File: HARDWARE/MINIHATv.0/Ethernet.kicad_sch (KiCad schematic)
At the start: 15 parts, among them J1 RJ45_Hanrun_HR911105A_Horizon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, U1 LAN8742A, Y1 Crystal_GND24_Small

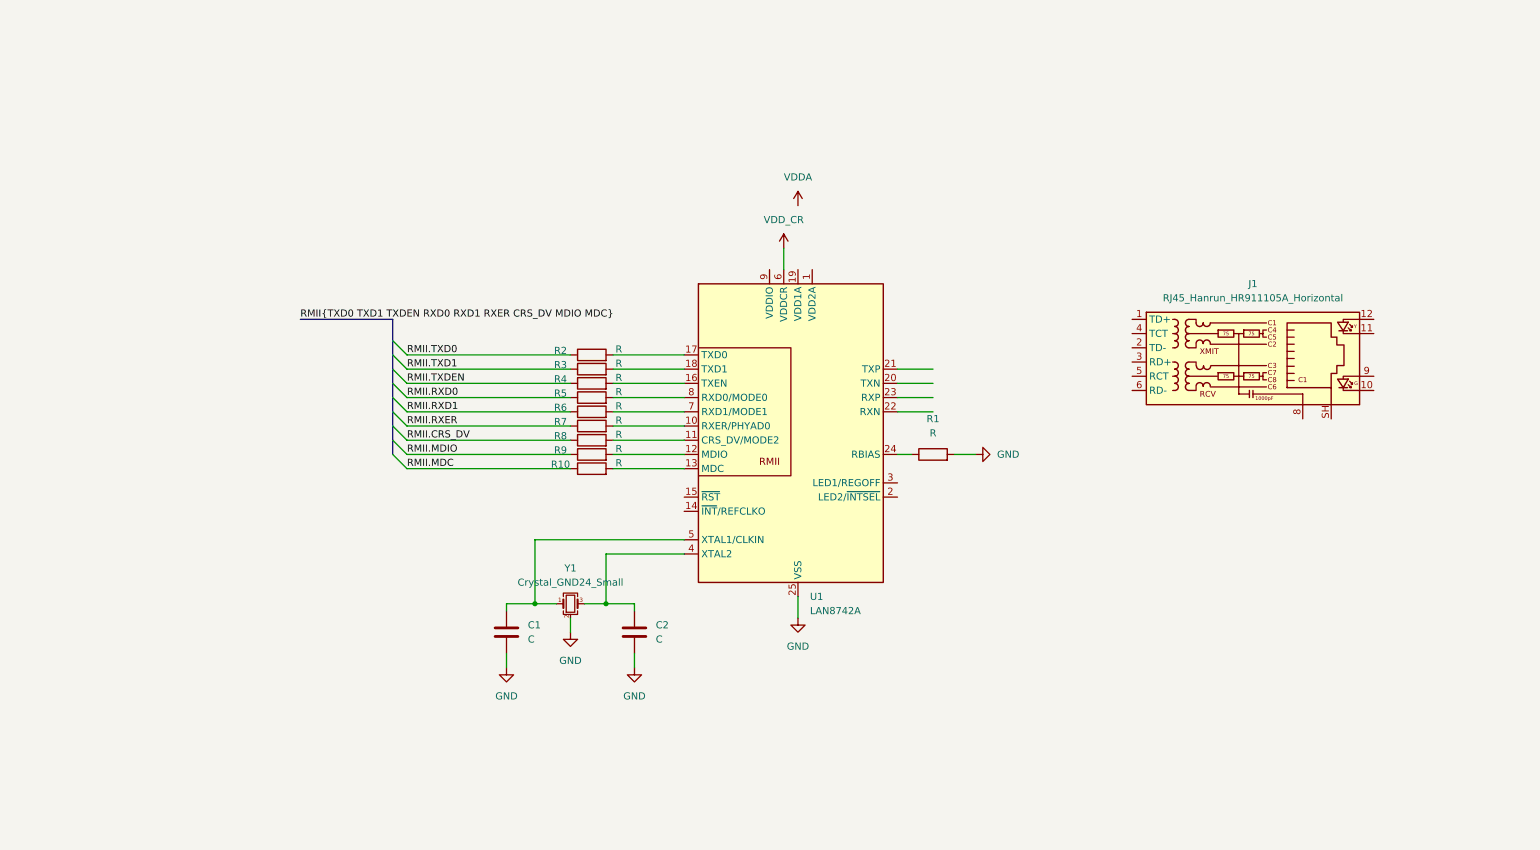
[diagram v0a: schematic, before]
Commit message: ethernet schematic complete
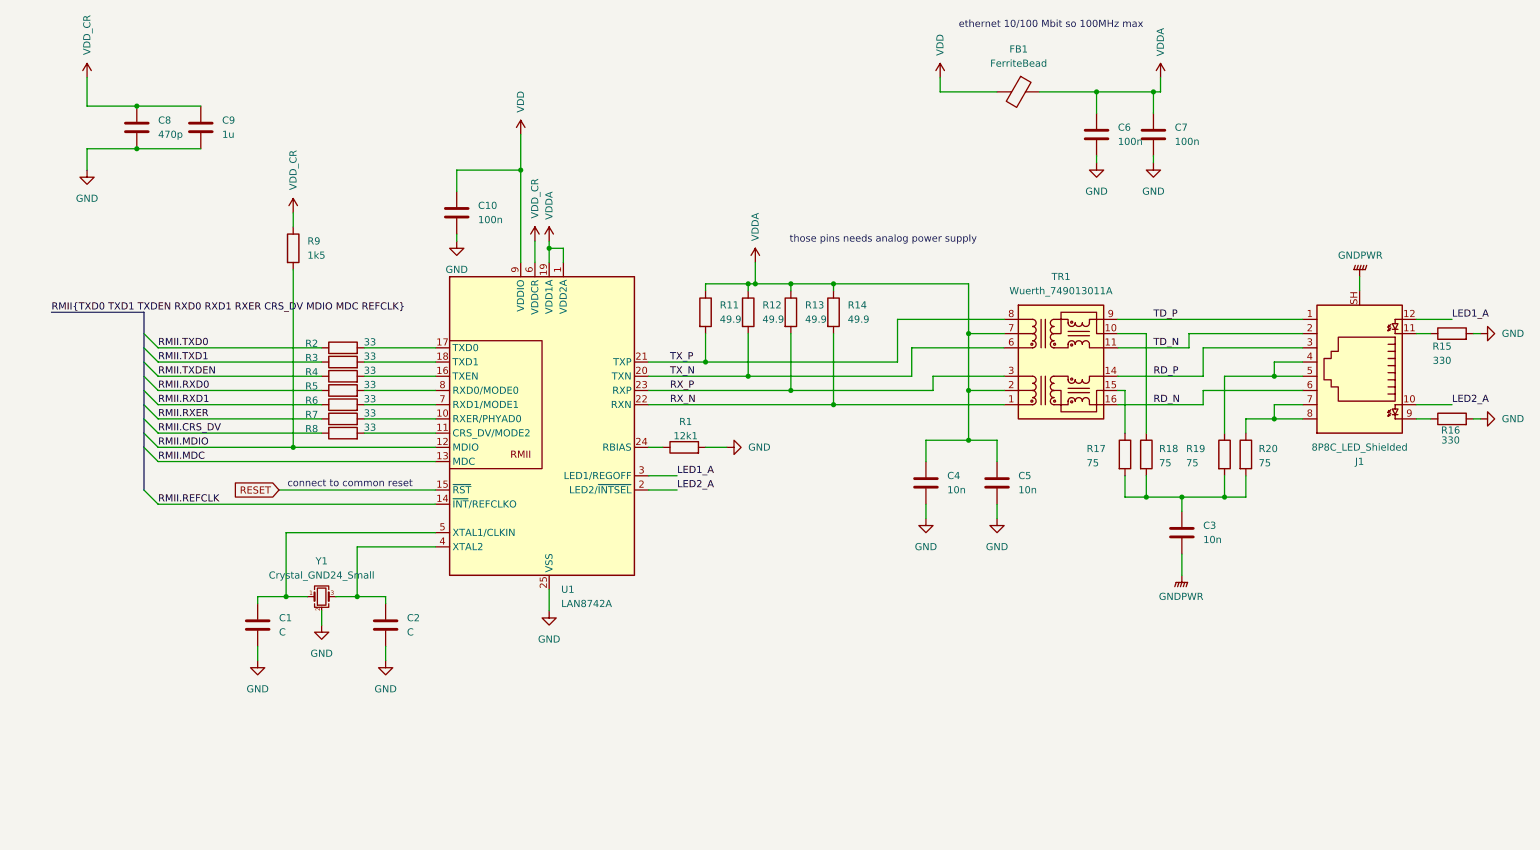
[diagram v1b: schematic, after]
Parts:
- removed J1: RJ45_Hanrun_HR911105A_Horizontal, Connector_RJ:RJ45_Amphenol_RJHSE538X, symbol Connector:RJ45_Hanrun_HR911105A_Horizontal
- removed R10: R, symbol Device:R
- added C10, C6, C7: 100n, symbol Device:C
- added C3, C4, C5: 10n, symbol Device:C
- added C8: 470p, symbol Device:C
- added C9: 1u, symbol Device:C
- added FB1: FerriteBead, symbol Device:FerriteBead
- added J1: 8P8C_LED_Shielded, symbol Connector:8P8C_LED_Shielded
- added R11, R12, R13, R14: 49.9, symbol Device:R
- added R15, R16: 330, symbol Device:R
- added R17, R18, R19, R20: 75, symbol Device:R
- added TR1: Wuerth_749013011A, Transformer_SMD:Transformer_Ethernet_Wuerth_749013011A, symbol Transformer:Wuerth_749013011A
- R1: value R -> 12k1
- R2, R3, R4, R5, R6, R7, R8: value R -> 33
- R9: value R -> 1k5
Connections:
- net GND: now also C10.2, C4.2, C5.2, C6.2, C7.2, C8.2, C9.2, R15.2, R16.2
- net RMII.MDC: now also U1.13 (MDC)
- net RMII.MDIO: now also R9.2, U1.12 (MDIO); no longer R9.1
- net VDDA: now also U1.1 (VDD2A), U1.19 (VDD1A), C4.1, C5.1, C6.1, C7.1, FB1.1, R11.1, R12.1, R13.1, R14.1, TR1.2 (C_TD), TR1.7 (C_RD)
- net VDD_CR: now also R9.1, C8.1, C9.1
- net RMII.REFCLK: now reaches U1.14 (~{INT}/REFCLKO)
- net RESET: now reaches U1.15 (~{RST})
- net LED2_A: now reaches U1.2 (LED2/~{INTSEL})
- net LED2_A: now also J1.10
- net TX_N: now reaches U1.20 (TXN)
- net TX_N: now also R12.2, TR1.6 (RD+)
- net TX_P: now reaches U1.21 (TXP)
- net TX_P: now also R11.2, TR1.8 (RD-)
- net RX_N: now reaches U1.22 (RXN)
- net RX_N: now also R14.2, TR1.1 (TD+)
- net RX_P: now reaches U1.23 (RXP)
- net RX_P: now also R13.2, TR1.3 (TD-)
- net LED1_A: now reaches U1.3 (LED1/REGOFF)
- net LED1_A: now also J1.12
- net VDD: now reaches U1.9 (VDDIO)
- net VDD: now also C10.1, FB1.2
- new net: R18.1, TR1.10 (C_RX)
- new net: R17.1, TR1.15 (C_TX)
- new net: C3.1, R17.2, R18.2, R19.2, R20.2
- new net: J1.7, J1.8, R20.1
- new net: J1.4, J1.5, R19.1
- new net: J1.11, R15.1
- new net: J1.9, R16.1
- new net GNDPWR: C3.2, J1.SH
- new net RD_N: J1.6, TR1.16 (TX+)
- new net RD_P: J1.3, TR1.14 (TX-)
- new net TD_N: J1.2, TR1.11 (RX+)
- new net TD_P: J1.1, TR1.9 (RX-)
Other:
- note added: "connect to common reset"
- note added: "ethernet 10/100 Mbit so 100MHz max"
- note added: "those pins needs analog power supply"
- moved on the sheet: C1, C2, R1, R2, R3, R4, R5, R6, R7, R8, U1, Y1

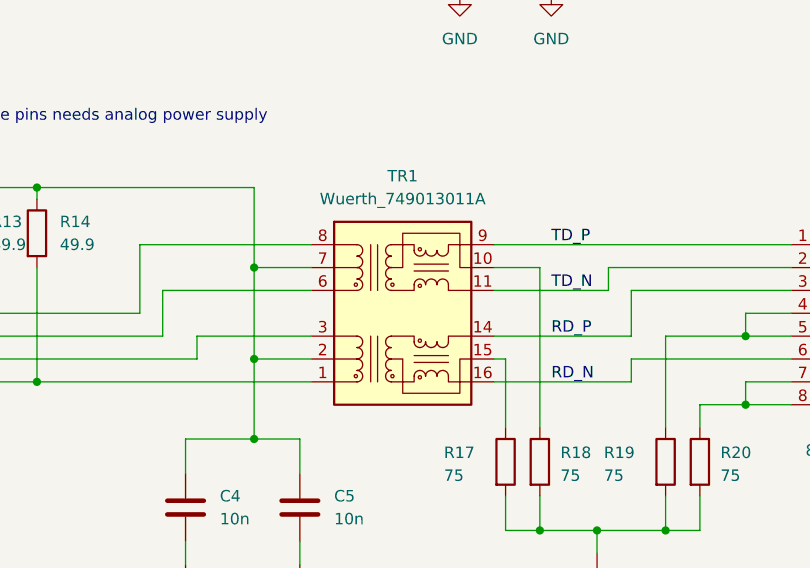
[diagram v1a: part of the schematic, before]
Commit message: added usb
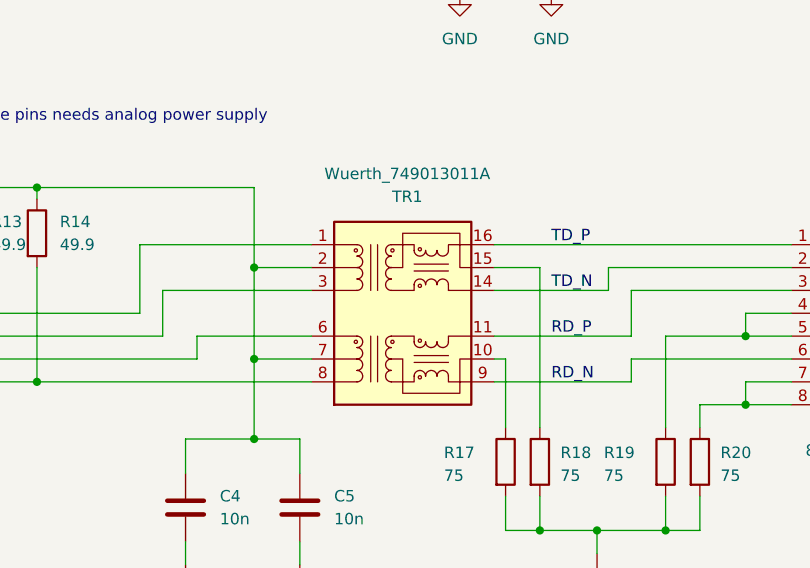
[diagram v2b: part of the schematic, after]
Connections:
- net RD_N: now also TR1.9 (RX-); no longer TR1.16 (TX+)
- net RD_P: now also TR1.11 (RX+); no longer TR1.14 (TX-)
- net RX_N: now also TR1.8 (RD-); no longer TR1.1 (TD+)
- net RX_P: now also TR1.6 (RD+); no longer TR1.3 (TD-)
- net TD_N: now also TR1.14 (TX-); no longer TR1.11 (RX+)
- net TD_P: now also TR1.16 (TX+); no longer TR1.9 (RX-)
- net TX_N: now also TR1.3 (TD-); no longer TR1.6 (RD+)
- net TX_P: now also TR1.1 (TD+); no longer TR1.8 (RD-)
- net at TR1.10 (C_RX): now also R17.1; no longer R18.1
- net at TR1.15 (C_TX): now also R18.1; no longer R17.1
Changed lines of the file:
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@@
+	)
+	(junction
+		(at 69.85 121.92)
+		(diameter 0)
+		(color 0 0 0 0)
+	)
+	(junction
+		(at 99.06 45.72)
+		(diameter 0)
+		(color 0 0 0 0)
+	)
+	(junction
+		(at 210.82 104.14)
+		(diameter 0)
+		(color 0 0 0 0)
 	)
 	(junction
@@
 	)
 	(junction
-		(at 69.85 121.92)
-		(diameter 0)
-		(color 0 0 0 0)
-	)
-	(junction
-		(at 99.06 45.72)
-		(diameter 0)
-		(color 0 0 0 0)
-	)
-	(junction
-		(at 210.82 104.14)
-		(diameter 0)
-		(color 0 0 0 0)
-	)
-	(junction
 		(at 147.32 66.04)
 		(diameter 0)
@@
 	)
 	(junction
+		(at 179.07 85.09)
+		(diameter 0)
+		(color 0 0 0 0)
+	)
+	(junction
 		(at 179.07 93.98)
 		(diameter 0)
@@
 	(junction
 		(at 154.94 66.04)
-		(diameter 0)
-		(color 0 0 0 0)
-	)
-	(junction
-		(at 179.07 85.09)
 		(diameter 0)
 		(color 0 0 0 0)
@@
 		(lib_id "Transformer:Wuerth_749013011A")
 		(at 195.58 80.01 0)
+		(mirror x)
 		(unit 1)
 		(body_style 1)
@@
 		(in_pos_files yes)
 		(dnp no)
-		(fields_autoplaced yes)
 		(property "Reference" "TR1"
-			(at 195.58 64.77 0)
+			(at 196.088 67.056 0)
 			(show_name no)
 			(do_not_autoplace no)
@@
 		)
 		(property "Value" "Wuerth_749013011A"
-			(at 195.58 67.31 0)
+			(at 196.088 64.516 0)
 			(show_name no)
 			(do_not_autoplace no)
@@
 		)
 		(property "Footprint" "Transformer_SMD:Transformer_Ethernet_Wuerth_749013011A"
-			(at 195.58 92.71 0)
+			(at 195.58 67.31 0)
 			(hide yes)
 			(show_name no)
@@
 		)
 		(property "Datasheet" "https://www.we-online.com/katalog/datasheet/749013011A.pdf"
-			(at 195.58 67.31 0)
+			(at 195.58 92.71 0)
 			(hide yes)
 			(show_name no)

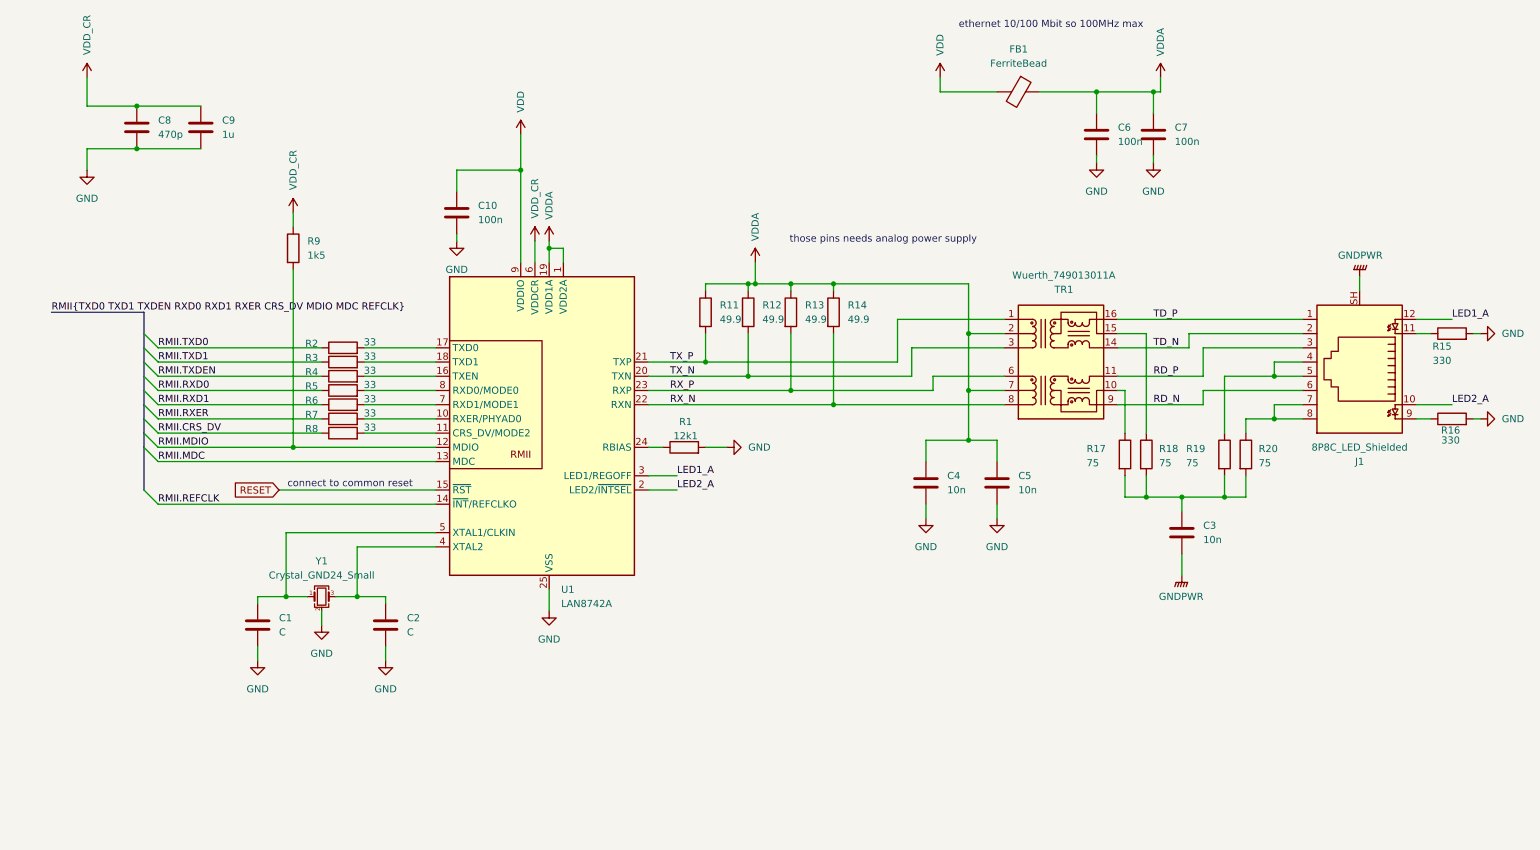
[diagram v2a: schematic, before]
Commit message: added normal buses
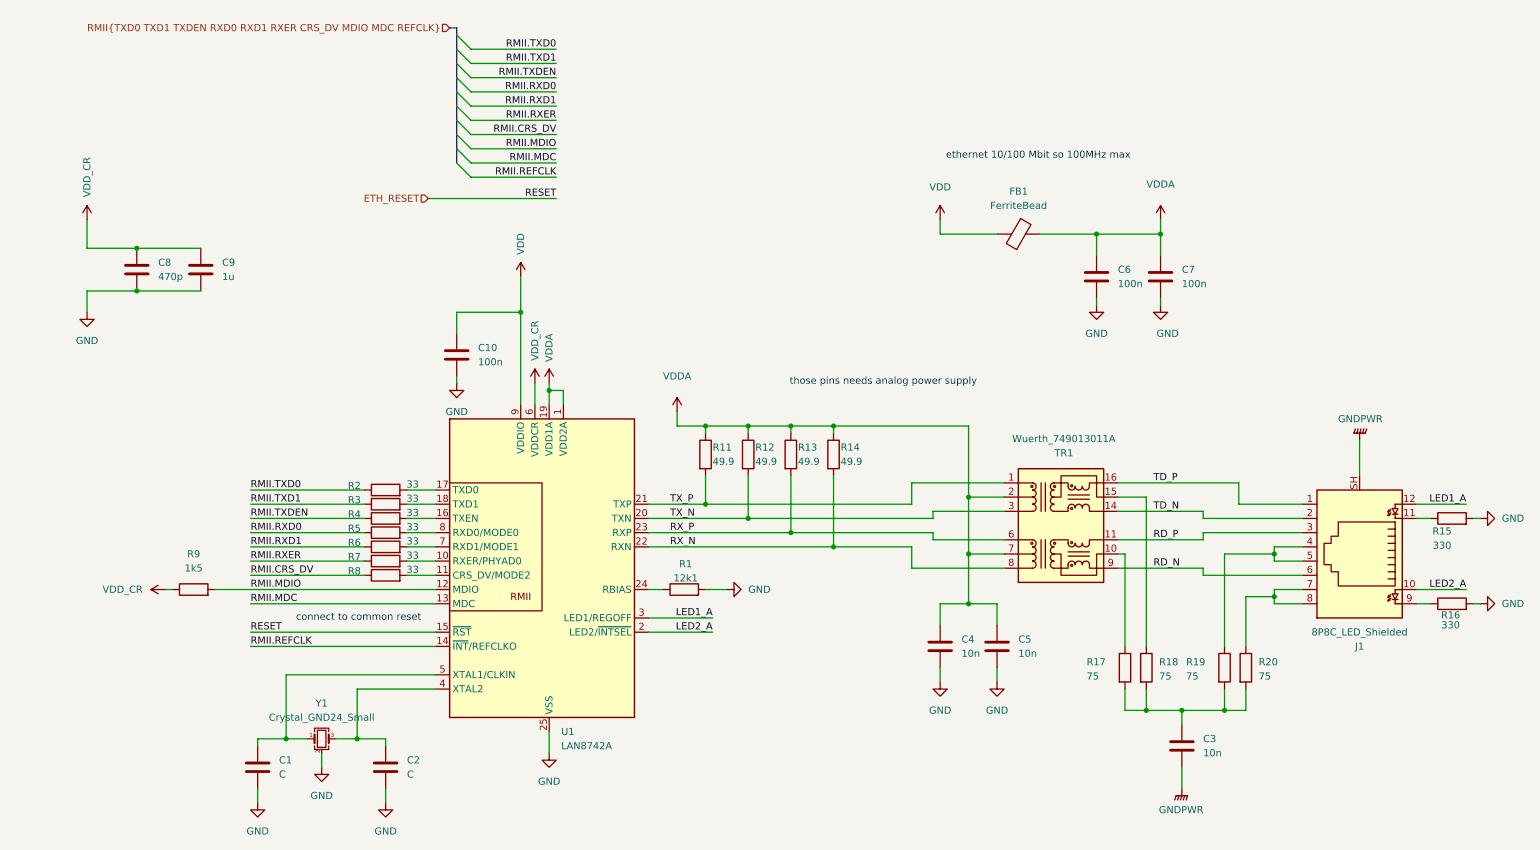
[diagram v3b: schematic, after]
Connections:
- net RESET renamed ETH_RESET
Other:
- moved on the sheet: C1, C10, C2, C3, C4, C5, C6, C7, C8, C9, FB1, J1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
